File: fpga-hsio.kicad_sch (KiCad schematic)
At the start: 3 parts, among them U1 MPFS250T-FCVG484, Y5 Oscillator_50MHz_ECS_1612MV

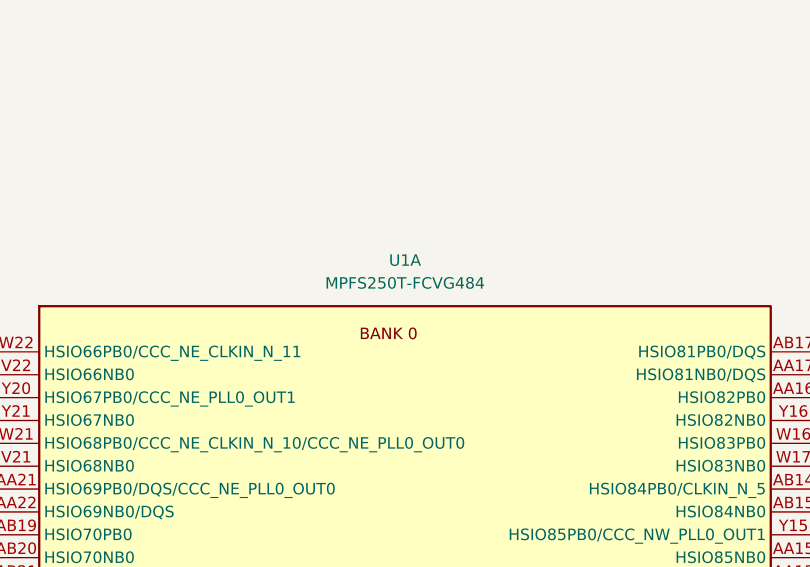
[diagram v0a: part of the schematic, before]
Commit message: [#76827] Update PolarFire MPN. Add test points. Modify DEVRST_N sequence. Bump revision
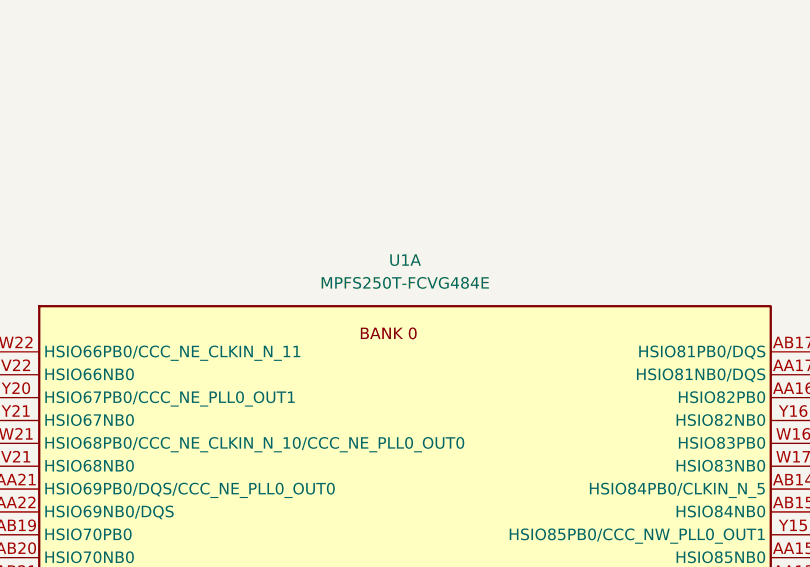
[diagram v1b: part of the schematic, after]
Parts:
- U1: footprint antmicro-footprints:BGA-484_19x19mm_Layout22x22_P0.8mm-microchip-technology-mpfs250t-fcvg484 -> antmicro-footprints:BGA-484_19x19mm_Layout22x22_P0.8mm_FCVG484; symbol antmicroFPGAChips:MPFS250T-FCVG484 -> antmicroFPGAChips:MPFS250T-FCVG484E; MPN MPFS250T-FCVG484 -> MPFS250T-FCVG484E
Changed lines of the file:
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@@
 	(title_block
 		(title "PolarFire SoM")
-		(date "2025-03-25")
-		(rev "1.1.2")
+		(date "2025-04-30")
+		(rev "1.1.3")
 		(company "Antmicro Ltd")
 		(comment 1 "www.antmicro.com")
@@
 	)
 	(symbol
-		(lib_id "antmicroFPGAChips:MPFS250T-FCVG484")
+		(lib_id "antmicroFPGAChips:MPFS250T-FCVG484E")
 		(at 177.8 77.47 0)
 		(unit 1)
@@
 			)
 		)
-		(property "Footprint" "antmicro-footprints:BGA-484_19x19mm_Layout22x22_P0.8mm-microchip-technology-mpfs250t-fcvg484"
+		(property "Footprint" "antmicro-footprints:BGA-484_19x19mm_Layout22x22_P0.8mm_FCVG484"
 			(at 283.21 85.09 0)
 			(effects
@@
 			)
 		)
-		(property "Datasheet" "https://www.microsemi.com/document-portal/doc_download/1244583-polarfire-soc-advance-datasheet"
+		(property "Datasheet" "https://ww1.microchip.com/downloads/aemDocuments/documents/FPGA/ProductDocuments/DataSheets/PolarFire-SoC-Datasheet-DS00004248.pdf"
 			(at 283.21 87.63 0)
 			(effects
@@
 		)
 		(property "Description" "RISC-V System On Chip (SOC) IC PolarFire® FPGA - 254K Logic Modules 484-FCBGA (19x19)"
-			(at 177.8 77.47 0)
+			(at 283.21 97.79 0)
 			(effects
 				(font
 					(size 1.27 1.27)
 				)
+				(justify left bottom)
 				(hide yes)
 			)
 		)
-		(property "MPN" "MPFS250T-FCVG484"
+		(property "MPN" "MPFS250T-FCVG484E"
 			(at 223.52 69.85 0)
 			(effects
